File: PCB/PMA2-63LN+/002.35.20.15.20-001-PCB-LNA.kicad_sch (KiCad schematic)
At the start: 12 parts, among them J1 Conn_Coaxial, J2 Conn_Coaxial, J3 Conn_Coaxial, U3 YAT-1A+, U4 L7805, U5 L7805

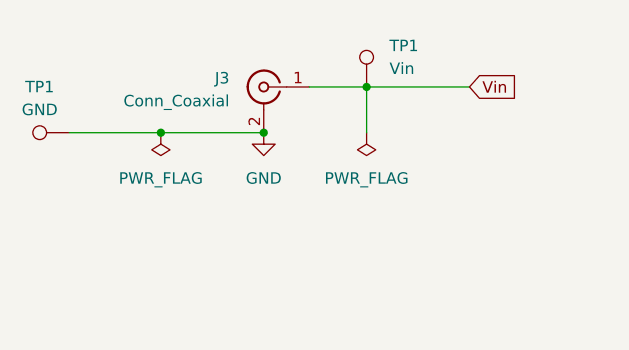
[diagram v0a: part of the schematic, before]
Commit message: pcb: added boms, updated readmes, changed silkscreen from dfs/ems to nmsm
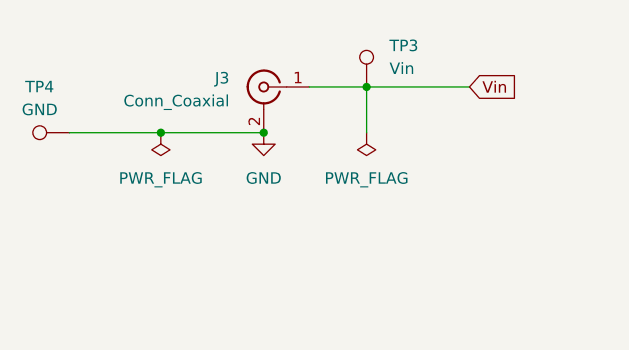
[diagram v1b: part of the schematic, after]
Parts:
- C10, C11, C12, C9: Link (none) -> https://www.digikey.com/en/products/detail/murata-electroni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
- J1, J2, J3: Link (none) -> https://www.digikey.com/en/products/detail/cinch-connectivi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
- TP3, TP4: renamed from TP1; Link (none) -> https://www.digikey.com/en/products/detail/keystone-electro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
- U3: Link (none) -> https://www.minicircuits.com/WebStore/dashboard.html?model=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
- U4, U5: Link (none) -> https://www.digikey.com/en/products/detail/stmicroelectroni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
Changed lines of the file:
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@@
+      (effects (font (size 1.27 1.27)) hide)
+    )
+    (property "Link" "https://www.digikey.com/en/products/detail/murata-electronics/GRM155R71H104KE14D/4906220" (at 242.57 50.8 0)
       (effects (font (size 1.27 1.27)) hide)
     )
@@
   (symbol (lib_id "rf-dfs:TestPoint") (at 48.26 50.8 90) (unit 1)
     (in_bom yes) (on_board yes) (dnp no) (fields_autoplaced)
-    (property "Reference" "TP1" (at 44.958 45.72 90)
+    (property "Reference" "TP4" (at 44.958 45.72 90)
       (effects (font (size 1.27 1.27)))
     )
@@
       (effects (font (size 1.27 1.27)) hide)
     )
-    (pin "1")
-    (instances
-      (project "002.35.20.15.20-001-PCB-LNA"
-        (path "/a33db424-96f2-4015-ba95-8b9f2330ef17/9ff85c99-1040-4eb9-b5d8-3cc01caa0e77"
-          (reference "TP1") (unit 1)
-        )
-        (path "/a33db424-96f2-4015-ba95-8b9f2330ef17/ba672304-1315-4178-9e1d-d553703e5b04"
-          (reference "TP2") (unit 1)
-        )
+    (property "Link" "https://www.digikey.com/en/products/detail/keystone-electronics/5006/255330" (at 48.26 50.8 0)
+      (effects (font (size 1.27 1.27)) hide)
+    )
+    (pin "1")
+    (instances
+      (project "002.35.20.15.20-001-PCB-LNA"
         (path "/a33db424-96f2-4015-ba95-8b9f2330ef17"
           (reference "TP4") (unit 1)
@@
       (effects (font (size 1.27 1.27)) hide)
     )
+    (property "Link" "https://www.digikey.com/en/products/detail/stmicroelectronics/L7805CD2T-TR/585695" (at 223.52 45.72 0)
+      (effects (font (size 1.27 1.27)) hide)
+    )
     (pin "1")
     (pin "2")
@@
       (effects (font (size 1.27 1.27)) hide)
     )
+    (property "Link" "https://www.digikey.com/en/products/detail/cinch-connectivity-solutions-johnson/142-0701-841/396573" (at 69.85 45.72 0)
+      (effects (font (size 1.27 1.27)) hide)
+    )
     (pin "1")
     (pin "2")
@@
       (effects (font (size 1.27 1.27)) hide)
     )
+    (property "Link" "https://www.digikey.com/en/products/detail/stmicroelectronics/L7805CD2T-TR/585695" (at 152.4 45.72 0)
+      (effects (font (size 1.27 1.27)) hide)
+    )
     (pin "1")
     (pin "2")
@@
       (effects (font (size 1.27 1.27)) hide)
     )
+    (property "Link" "https://www.digikey.com/en/products/detail/murata-electronics/GRM155R61H334KE01J/19115579" (at 200.66 50.8 0)
+      (effects (font (size 1.27 1.27)) hide)
+    )
     (pin "1")
     (pin "2")
@@
       (effects (font (size 1.27 1.27)) hide)
     )
+    (property "Link" "https://www.digikey.com/en/products/detail/murata-electronics/GRM155R71H104KE14D/4906220" (at 171.45 50.8 0)
+      (effects (font (size 1.27 1.27)) hide)
+    )
     (pin "1")
     (pin "2")
@@
     )
     (property "Datasheet" "~" (at 129.54 50.8 0)
+      (effects (font (size 1.27 1.27)) hide)
+    )
+    (property "Link" "https://www.digikey.com/en/products/detail/murata-electronics/GRM155R61H334KE01J/19115579" (at 129.54 50.8 0)
       (effects (font (size 1.27 1.27)) hide)
     )
@@
     (property "Datasheet" "YAT-1A+" (at 124.46 121.92 0)
       (effects (font (size 1.27 1.27) italic) hide)
+    )
+    (property "Link" "https://www.minicircuits.com/WebStore/dashboard.html?model=YAT-1A%2B" (at 124.46 121.92 0)
+      (effects (font (size 1.27 1.27)) hide)
     )
     (pin "2")
@@
       (effects (font (size 1.27 1.27)) hide)
     )
+    (property "Link" "https://www.digikey.com/en/products/detail/cinch-connectivity-solutions-johnson/142-0701-841/396573" (at 60.96 124.46 0)
+      (effects (font (size 1.27 1.27)) hide)
+    )
     (pin "1")
     (pin "2")
@@
       (effects (font (size 1.27 1.27)) hide)
     )
+    (property "Link" "https://www.digikey.com/en/products/detail/cinch-connectivity-solutions-johnson/142-0701-841/396573" (at 245.11 127 0)
+      (effects (font (size 1.27 1.27)) hide)
+    )
     (pin "1")
     (pin "2")
@@
   (symbol (lib_id "rf-dfs:TestPoint") (at 81.28 45.72 0) (unit 1)
     (in_bom yes) (on_board yes) (dnp no) (fields_autoplaced)
-    (property "Reference" "TP1" (at 83.82 41.148 0)
+    (property "Reference" "TP3" (at 83.82 41.148 0)
       (effects (font (size 1.27 1.27)) (justify left))
     )
@@
       (effects (font (size 1.27 1.27)) hide)
     )
-    (pin "1")
-    (instances
-      (project "002.35.20.15.20-001-PCB-LNA"
-        (path "/a33db424-96f2-4015-ba95-8b9f2330ef17/9ff85c99-1040-4eb9-b5d8-3cc01caa0e77"
-          (reference "TP1") (unit 1)
-        )
-        (path "/a33db424-96f2-4015-ba95-8b9f2330ef17/ba672304-1315-4178-9e1d-d553703e5b04"
-          (reference "TP2") (unit 1)
-        )
+    (property "Link" "https://www.digikey.com/en/products/detail/keystone-electronics/5005/255329" (at 81.28 45.72 0)
+      (effects (font (size 1.27 1.27)) hide)
+    )
+    (pin "1")
+    (instances
+      (project "002.35.20.15.20-001-PCB-LNA"
         (path "/a33db424-96f2-4015-ba95-8b9f2330ef17"
           (reference "TP3") (unit 1)
